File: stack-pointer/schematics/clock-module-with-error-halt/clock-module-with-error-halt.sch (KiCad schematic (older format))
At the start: 23 parts, among them SW1 SW_Push, SW2 SW_SPDT, U1 LM555, U2 LM556, U4 74LS04, U5 74LS08, U6 74LS32

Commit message: small iteration on schematics
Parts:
- added U3: 74LS32, symbol 74xx:74LS32
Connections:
- net ERR_SPO: now also U3.1; no longer U6.10
- new net: U3.3, U6.10
- new net ERR_NXO: U3.2
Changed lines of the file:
@@
 U 2 1 5B5312F6
 P 3000 5900
-F 0 "U6" H 3000 5950 50  0000 C CNN
-F 1 "74LS32" H 3000 5850 50  0000 C CNN
+F 0 "U6" H 3000 5900 50  0000 C CNN
+F 1 "74LS32" H 3250 6025 50  0000 C CNN
 F 2 "Package_DIP:DIP-14_W7.62mm" H 3000 5900 50  0001 C CNN
 F 3 "" H 3000 5900 50  0001 C CNN
@@
 U 3 1 5B5313CF
 P 3000 6450
-F 0 "U6" H 3000 6500 50  0000 C CNN
-F 1 "74LS32" H 3000 6400 50  0000 C CNN
+F 0 "U6" H 3000 6450 50  0000 C CNN
+F 1 "74LS32" H 3275 6350 50  0000 C CNN
 F 2 "Package_DIP:DIP-14_W7.62mm" H 3000 6450 50  0001 C CNN
 F 3 "" H 3000 6450 50  0001 C CNN
@@
 U 4 1 5B531491
 P 3600 6150
-F 0 "U6" H 3600 6200 50  0000 C CNN
-F 1 "74LS32" H 3600 6100 50  0000 C CNN
+F 0 "U6" H 3600 6150 50  0000 C CNN
+F 1 "74LS32" H 3875 6050 50  0000 C CNN
 F 2 "Package_DIP:DIP-14_W7.62mm" H 3600 6150 50  0001 C CNN
 F 3 "" H 3600 6150 50  0001 C CNN
@@
 	1450 6000 2700 6000
 Wire Wire Line
-	1450 6550 2700 6550
-Wire Wire Line
 	3300 6450 3300 6250
 Wire Wire Line
@@
 Wire Wire Line
 	5900 4800 6700 4800
+$Comp
+L 74xx:74LS32 U3
+U 1 1 61846556
+P 2075 6650
+F 0 "U3" H 2075 6650 50  0000 C CNN
+F 1 "74LS32" H 2325 6525 50  0000 C CNN
+F 2 "" H 2075 6650 50  0001 C CNN
+F 3 "http://www.ti.com/lit/gpn/sn74LS32" H 2075 6650 50  0001 C CNN
+	1    2075 6650
+	1    0    0    -1
+$EndComp
+Text HLabel 1450 6750 0    50   Input ~ 0
+ERR_NXO
+Wire Wire Line
+	1450 6750 1775 6750
+Wire Wire Line
+	1450 6550 1775 6550
+Wire Wire Line
+	2375 6650 2500 6650
+Wire Wire Line
+	2500 6650 2500 6550
+Wire Wire Line
+	2500 6550 2700 6550
 $EndSCHEMATC

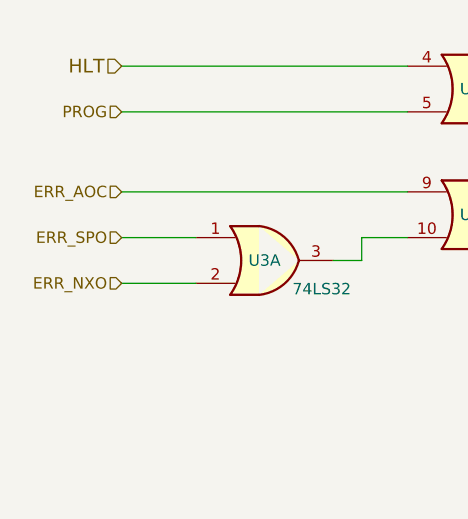
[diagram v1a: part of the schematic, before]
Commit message: updated index register symbol
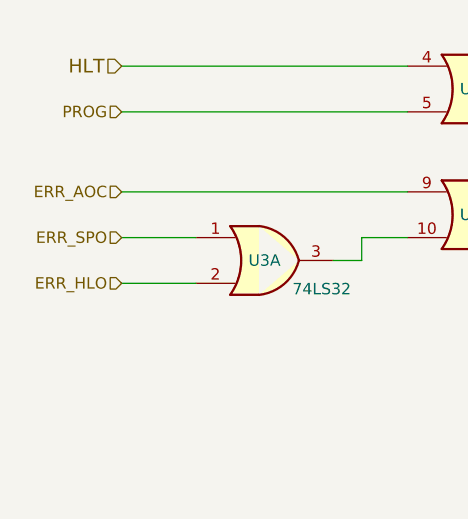
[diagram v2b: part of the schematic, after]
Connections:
- net ERR_NXO renamed ERR_HLO
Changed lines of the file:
@@
 $EndComp
 Text HLabel 1450 6750 0    50   Input ~ 0
-ERR_NXO
+ERR_HLO
 Wire Wire Line
 	1450 6750 1775 6750

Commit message: removed stack pointer and index register error flags
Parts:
- removed U3: 74LS32, symbol 74xx:74LS32
- removed unit 4 of U4
- removed unit 6 of U4
- removed unit 5 of U4
- removed unit 4 of U5
- removed unit 3 of U6
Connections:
- net ERR_AOC: now also U6.9
- net HLT: now also U6.12; no longer U6.4
- net PROG: now also U6.13; no longer U6.5
- net at U4.3: now also U6.8; no longer U6.11
- new net: U6.10, U6.11
- no-connect marks 11 -> 2
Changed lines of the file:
@@
-	1    0    0    -1
-$EndComp
-$Comp
-L 74xx:74LS04 U4
-U 4 1 5B52E7BF
-P 4400 7525
-F 0 "U4" H 4595 7640 50  0000 C CNN
-F 1 "74LS04" H 4590 7400 50  0000 C CNN
-F 2 "Package_DIP:DIP-14_W7.62mm" H 4400 7525 50  0001 C CNN
-F 3 "" H 4400 7525 50  0001 C CNN
-	4    4400 7525
-	1    0    0    -1
-$EndComp
-$Comp
-L 74xx:74LS04 U4
-U 6 1 5B52E82B
-P 6000 7525
-F 0 "U4" H 6195 7640 50  0000 C CNN
-F 1 "74LS04" H 6190 7400 50  0000 C CNN
-F 2 "Package_DIP:DIP-14_W7.62mm" H 6000 7525 50  0001 C CNN
-F 3 "" H 6000 7525 50  0001 C CNN
-	6    6000 7525
 	1    0    0    -1
 $EndComp
@@
 $EndComp
 $Comp
-L 74xx:74LS04 U4
-U 5 1 5B53108F
-P 5200 7525
-F 0 "U4" H 5395 7640 50  0000 C CNN
-F 1 "74LS04" H 5390 7400 50  0000 C CNN
-F 2 "Package_DIP:DIP-14_W7.62mm" H 5200 7525 50  0001 C CNN
-F 3 "" H 5200 7525 50  0001 C CNN
-	5    5200 7525
-	1    0    0    -1
-$EndComp
-$Comp
-L 74xx:74LS08 U5
-U 4 1 5B53125C
-P 6000 6925
-F 0 "U5" H 6000 6975 50  0000 C CNN
-F 1 "74LS08" H 6000 6875 50  0000 C CNN
-F 2 "Package_DIP:DIP-14_W7.62mm" H 6000 6925 50  0001 C CNN
-F 3 "" H 6000 6925 50  0001 C CNN
-	4    6000 6925
-	1    0    0    -1
-$EndComp
-$Comp
 L 74xx:74LS32 U6
-U 2 1 5B5312F6
+U 4 1 5B5312F6
 P 3000 5900
 F 0 "U6" H 3000 5900 50  0000 C CNN
@@
 F 2 "Package_DIP:DIP-14_W7.62mm" H 3000 5900 50  0001 C CNN
 F 3 "" H 3000 5900 50  0001 C CNN
-	2    3000 5900
-	1    0    0    -1
-$EndComp
-$Comp
-L 74xx:74LS32 U6
-U 3 1 5B5313CF
-P 3000 6450
-F 0 "U6" H 3000 6450 50  0000 C CNN
-F 1 "74LS32" H 3275 6350 50  0000 C CNN
-F 2 "Package_DIP:DIP-14_W7.62mm" H 3000 6450 50  0001 C CNN
-F 3 "" H 3000 6450 50  0001 C CNN
-	3    3000 6450
-	1    0    0    -1
-$EndComp
-NoConn ~ 5500 7525
-NoConn ~ 4900 7525
-NoConn ~ 4700 7525
-NoConn ~ 5700 6825
-NoConn ~ 5700 7025
-NoConn ~ 6300 6925
+	4    3000 5900
+	1    0    0    -1
+$EndComp
 Wire Wire Line
 	7950 2500 7950 2850
@@
 Wire Wire Line
 	9750 1850 9900 1850
-NoConn ~ 4100 7525
-NoConn ~ 5700 7525
-NoConn ~ 6300 7525
 Text HLabel 1450 6000 0    50   Input ~ 0
 PROG
 $Comp
 L 74xx:74LS32 U6
-U 4 1 5B531491
+U 3 1 5B531491
 P 3600 6150
 F 0 "U6" H 3600 6150 50  0000 C CNN
@@
 F 2 "Package_DIP:DIP-14_W7.62mm" H 3600 6150 50  0001 C CNN
 F 3 "" H 3600 6150 50  0001 C CNN
-	4    3600 6150
-	1    0    0    -1
+	3    3600 6150
+	1    0    0    1
 $EndComp
 $Comp
@@
 	1    0    0    -1
 $EndComp
-Text HLabel 1450 6350 0    50   Input ~ 0
+Text HLabel 1450 6250 0    50   Input ~ 0
 ERR_AOC
-Text HLabel 1450 6550 0    50   Input ~ 0
-ERR_SPO
-Wire Wire Line
-	1450 6350 2700 6350
 Wire Wire Line
 	1450 6000 2700 6000
 Wire Wire Line
-	3300 6450 3300 6250
-Wire Wire Line
 	3300 5900 3300 6050
 Wire Wire Line
@@
 Wire Wire Line
 	5900 4800 6700 4800
-$Comp
-L 74xx:74LS32 U3
-U 1 1 61846556
-P 2075 6650
-F 0 "U3" H 2075 6650 50  0000 C CNN
-F 1 "74LS32" H 2325 6525 50  0000 C CNN
-F 2 "" H 2075 6650 50  0001 C CNN
-F 3 "http://www.ti.com/lit/gpn/sn74LS32" H 2075 6650 50  0001 C CNN
-	1    2075 6650
-	1    0    0    -1
-$EndComp
-Text HLabel 1450 6750 0    50   Input ~ 0
-ERR_HLO
-Wire Wire Line
-	1450 6750 1775 6750
-Wire Wire Line
-	1450 6550 1775 6550
-Wire Wire Line
-	2375 6650 2500 6650
-Wire Wire Line
-	2500 6650 2500 6550
-Wire Wire Line
-	2500 6550 2700 6550
+Wire Wire Line
+	1450 6250 3300 6250
 $EndSCHEMATC
